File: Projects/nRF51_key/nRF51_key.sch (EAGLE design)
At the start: 4 parts, among them IC1 FT230XQ, X1 USBPCB

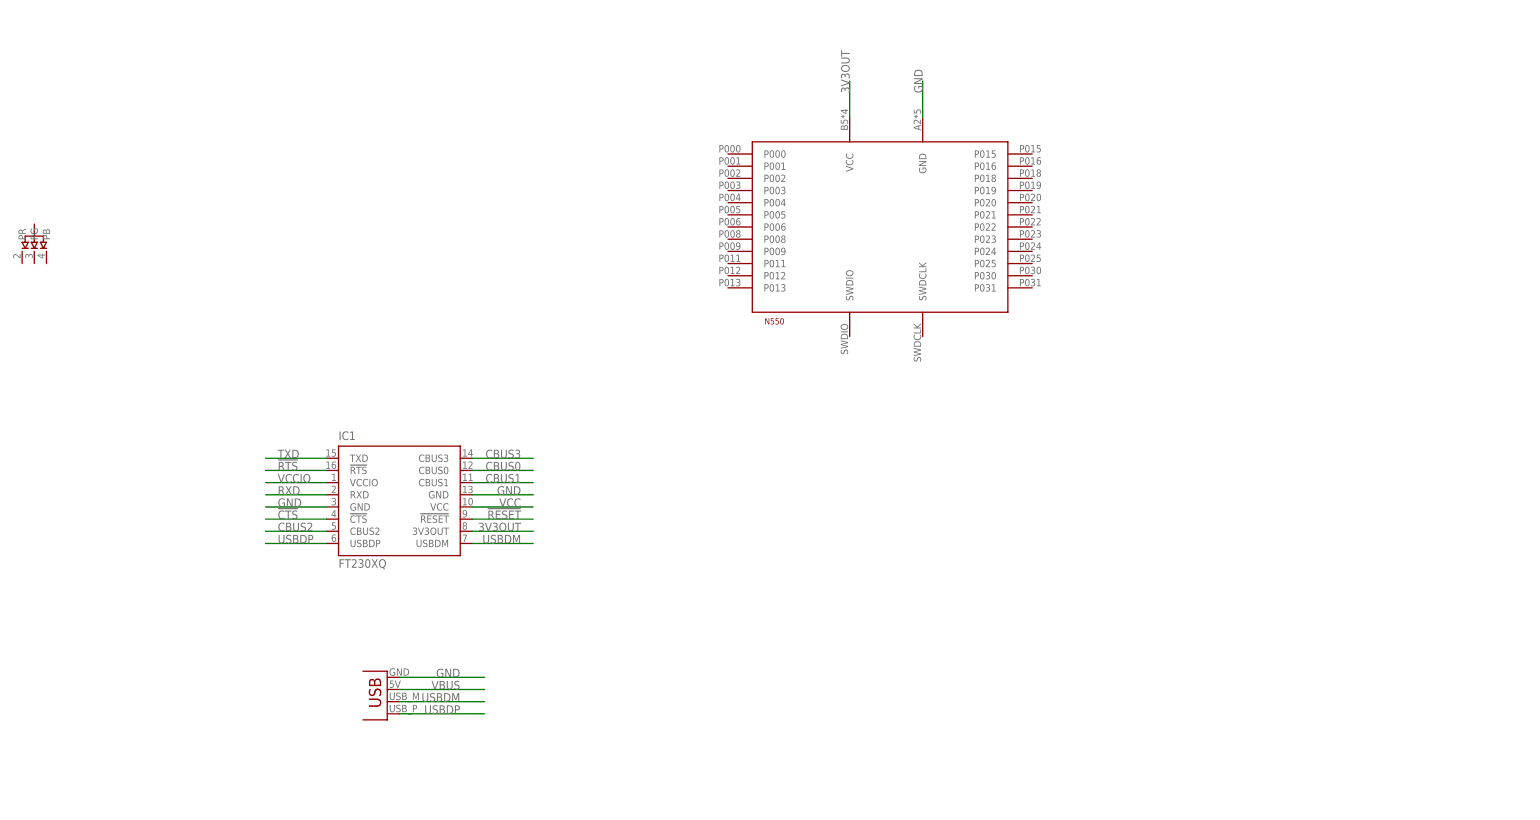
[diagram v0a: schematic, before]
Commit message: More on the nRF51 USB key
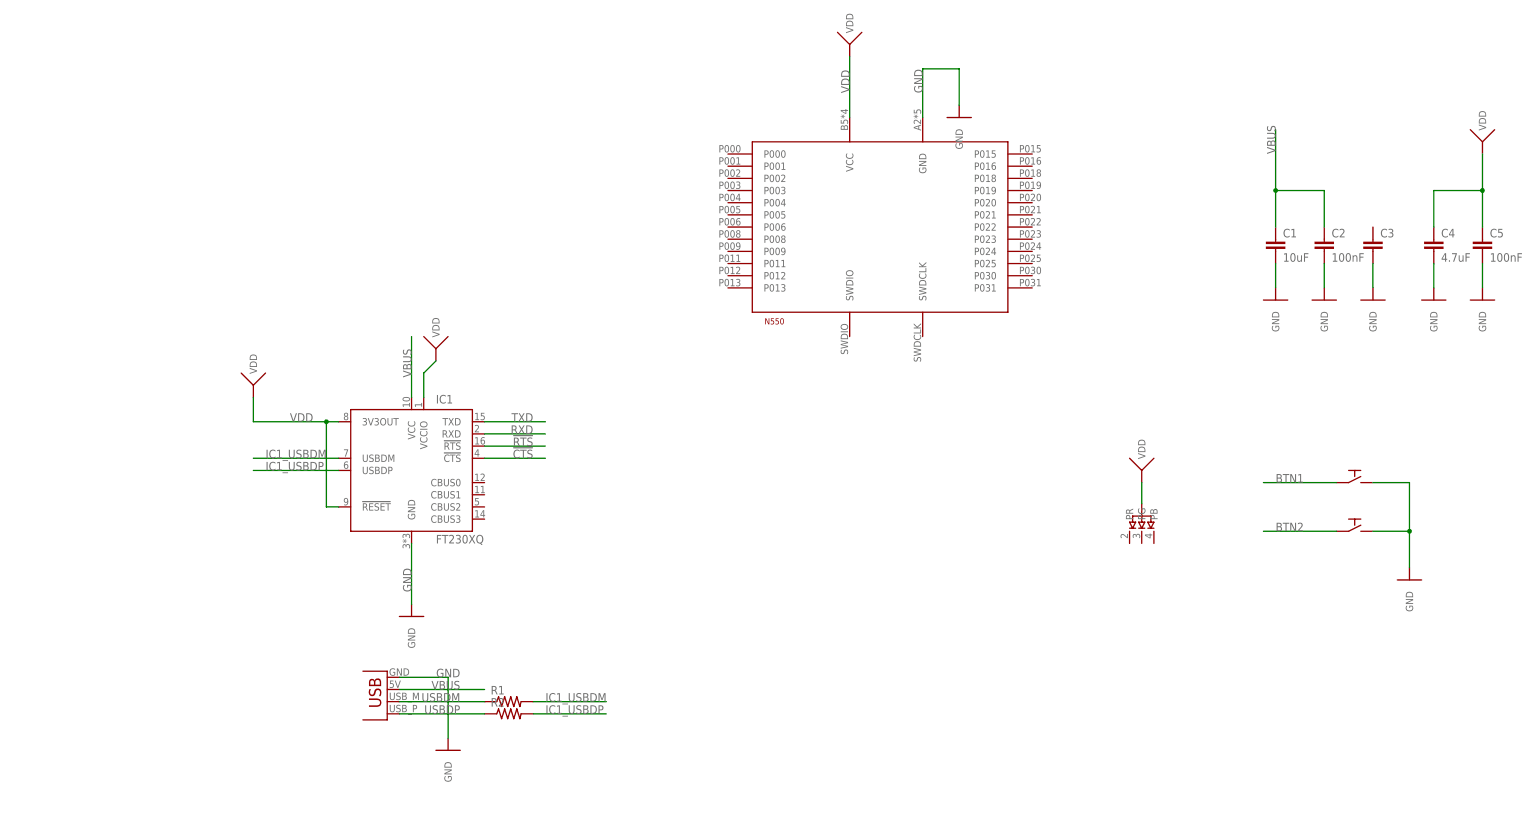
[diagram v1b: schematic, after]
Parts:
- added C1: 10uF, Passives:CAPACITOR0603
- added C2, C5: 100nF, Passives:CAPACITOR0603
- added C3: (no value), Passives:CAPACITOR0603
- added C4: 4.7uF, Passives:CAPACITOR0603
- added R1, R2: (no value), Passives:RESISTOR0603
- added SPST1, SPST2: PTS526SK08, SPST:PTS526SK08
- IC1: device ftdichip:FT230XQ -> FTDI:FT230XQ
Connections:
- removed net !RESET: IC1.!RESET
- removed net 3V3OUT: IC1.3V3OUT, U$1.VCC
- removed net CBUS0: IC1.CBUS0
- removed net CBUS1: IC1.CBUS1
- removed net CBUS2: IC1.CBUS2
- removed net CBUS3: IC1.CBUS3
- removed net VCC: IC1.VCC
- removed net VCCIO: IC1.VCCIO
- new net BTN1: SPST1.P$1
- new net BTN2: SPST2.P$1
- new net IC1_USBDM: IC1.USBDM, R1.2
- new net IC1_USBDP: IC1.USBDP, R2.2
- new net VDD: C4.1, C5.1, D1.P$1, IC1.!RESET, IC1.3V3OUT, IC1.VCCIO, U$1.VCC
- net GND: now also C1.2, C2.2, C3.2, C4.2, C5.2, SPST1.P$2, SPST2.P$2; no longer IC1.GND@1
- net USBDM: now also R1.1; no longer IC1.USBDM
- net USBDP: now also R2.1; no longer IC1.USBDP
- net VBUS: now also C1.1, C2.1, IC1.VCC

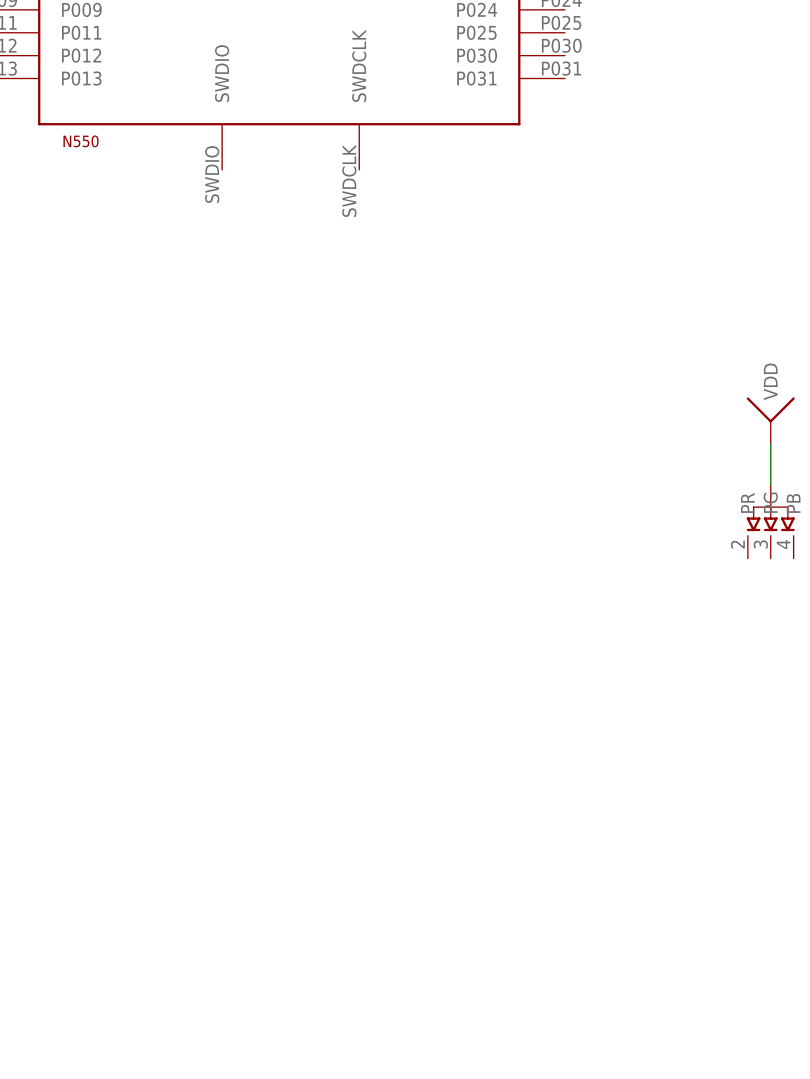
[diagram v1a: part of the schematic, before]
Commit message: Added PCB SD card symbol
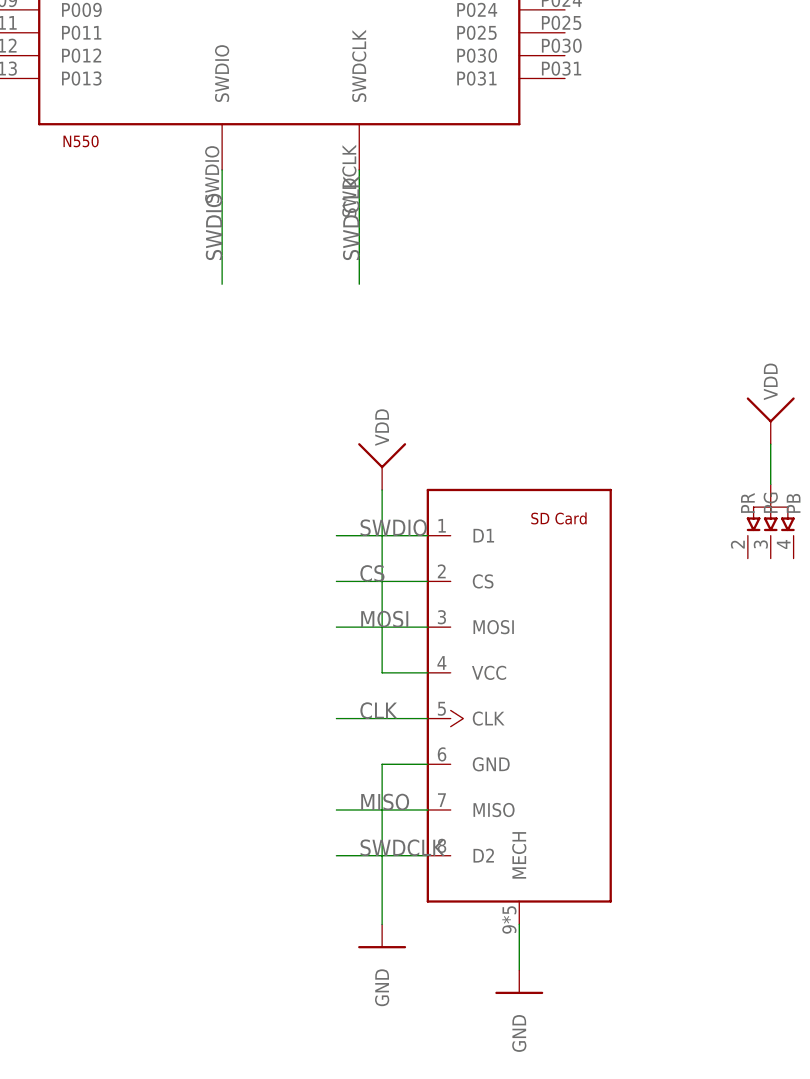
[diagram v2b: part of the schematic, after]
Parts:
- added J1: 47571-0001, SD_Card:47571-0001
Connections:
- new net CLK: J1.CLK
- new net CS: J1.CS
- new net MISO: J1.MISO
- new net MOSI: J1.MOSI
- new net SWDCLK: J1.D2, U$1.SWDCLK
- new net SWDIO: J1.D1, U$1.SWDIO
- net GND: now also J1.GND, J1.MECH
- net VDD: now also J1.VCC
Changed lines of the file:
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@@
 <layer number="54" name="bGND_GNDA" color="1" fill="9" visible="no" active="no"/>
 <layer number="56" name="wert" color="7" fill="1" visible="no" active="no"/>
+<layer number="57" name="tCAD" color="7" fill="1" visible="no" active="no"/>
+<layer number="59" name="tCarbon" color="7" fill="1" visible="no" active="no"/>
+<layer number="60" name="bCarbon" color="7" fill="1" visible="no" active="no"/>
 <layer number="88" name="SimResults" color="9" fill="1" visible="yes" active="yes"/>
 <layer number="89" name="SimProbes" color="9" fill="1" visible="yes" active="yes"/>
@@
 <layer number="125" name="_tNames" color="7" fill="1" visible="no" active="yes"/>
 <layer number="126" name="BIFRNTMAT" color="7" fill="1" visible="yes" active="yes"/>
+<layer number="127" name="_tValues" color="7" fill="1" visible="no" active="no"/>
+<layer number="128" name="_bValues" color="7" fill="1" visible="no" active="no"/>
+<layer number="129" name="Mask" color="7" fill="1" visible="no" active="no"/>
 <layer number="130" name="SMDSTROOK" color="7" fill="1" visible="yes" active="yes"/>
 <layer number="131" name="tAdjust" color="7" fill="1" visible="yes" active="yes"/>
 <layer number="132" name="bAdjust" color="7" fill="1" visible="yes" active="yes"/>
 <layer number="144" name="Drill_legend" color="7" fill="1" visible="no" active="yes"/>
+<layer number="150" name="Notes" color="7" fill="1" visible="no" active="no"/>
 <layer number="151" name="HeatSink" color="7" fill="1" visible="no" active="yes"/>
+<layer number="152" name="_bDocu" color="7" fill="1" visible="no" active="no"/>
+<layer number="153" name="FabDoc1" color="7" fill="1" visible="no" active="no"/>
+<layer number="154" name="FabDoc2" color="7" fill="1" visible="no" active="no"/>
+<layer number="155" name="FabDoc3" color="7" fill="1" visible="no" active="no"/>
 <layer number="199" name="Contour" color="7" fill="1" visible="yes" active="yes"/>
 <layer number="200" name="200bmp" color="1" fill="10" visible="no" active="yes"/>
@@
 <layer number="223" name="223bmp" color="24" fill="1" visible="no" active="no"/>
 <layer number="224" name="224bmp" color="25" fill="1" visible="no" active="no"/>
+<layer number="225" name="225bmp" color="7" fill="1" visible="no" active="no"/>
+<layer number="226" name="226bmp" color="7" fill="1" visible="no" active="no"/>
+<layer number="227" name="227bmp" color="7" fill="1" visible="no" active="no"/>
+<layer number="228" name="228bmp" color="7" fill="1" visible="no" active="no"/>
+<layer number="229" name="229bmp" color="7" fill="1" visible="no" active="no"/>
+<layer number="230" name="230bmp" color="7" fill="1" visible="no" active="no"/>
+<layer number="231" name="231bmp" color="7" fill="1" visible="no" active="no"/>
+<layer number="232" name="Eagle3D_PG2" color="7" fill="1" visible="no" active="no"/>
+<layer number="233" name="Eagle3D_PG3" color="7" fill="1" visible="no" active="no"/>
+<layer number="248" name="Housing" color="7" fill="1" visible="no" active="no"/>
+<layer number="249" name="Edge" color="7" fill="1" visible="no" active="no"/>
 <layer number="250" name="Descript" color="3" fill="1" visible="no" active="no"/>
 <layer number="251" name="SMDround" color="12" fill="11" visible="no" active="no"/>
@@
 <part name="R2" library="Passives" deviceset="RESISTOR" device="0603"/>
 <part name="U$15" library="PowerSupplies" deviceset="VDD" device=""/>
+<part name="J1" library="SD_Card" deviceset="47571-0001" device=""/>
+<part name="U$16" library="PowerSupplies" deviceset="GND" device=""/>
+<part name="U$17" library="PowerSupplies" deviceset="GND" device=""/>
+<part name="U$18" library="PowerSupplies" deviceset="VDD" device=""/>
 </parts>
 <sheets>
@@
 </instance>
 <instance part="U$15" gate="G$1" x="-50.8" y="2.54" smashed="yes"/>
+<instance part="J1" gate="G$1" x="68.58" y="-53.34" smashed="yes"/>
+<instance part="U$16" gate="GND" x="68.58" y="-86.36" smashed="yes"/>
+<instance part="U$17" gate="GND" x="53.34" y="-81.28" smashed="yes"/>
+<instance part="U$18" gate="G$1" x="53.34" y="-27.94" smashed="yes"/>
 </instances>
 <busses>
@@
 <pinref part="C1" gate="G$1" pin="2"/>
 <wire x1="124.46" y1="15.24" x2="124.46" y2="20.32" width="0.1524" layer="91" grouprefs="DECAP"/>
+</segment>
+<segment>
+<pinref part="J1" gate="G$1" pin="GND"/>
+<wire x1="58.42" y1="-60.96" x2="53.34" y2="-60.96" width="0.1524" layer="91"/>
+<pinref part="U$17" gate="GND" pin="GND"/>
+<wire x1="53.34" y1="-60.96" x2="53.34" y2="-78.74" width="0.1524" layer="91"/>
+</segment>
+<segment>
+<pinref part="J1" gate="G$1" pin="MECH"/>
+<pinref part="U$16" gate="GND" pin="GND"/>
+<wire x1="68.58" y1="-78.74" x2="68.58" y2="-83.82" width="0.1524" layer="91"/>
 </segment>
 </net>
@@
 <wire x1="-53.34" y1="-2.54" x2="-53.34" y2="-7.62" width="0.1524" layer="91"/>
 </segment>
+<segment>
+<pinref part="U$18" gate="G$1" pin="VDD"/>
+<wire x1="53.34" y1="-30.48" x2="53.34" y2="-50.8" width="0.1524" layer="91"/>
+<pinref part="J1" gate="G$1" pin="VCC"/>
+<wire x1="53.34" y1="-50.8" x2="58.42" y2="-50.8" width="0.1524" layer="91"/>
+</segment>
 </net>
 <net name="BTN1" class="0">
@@
 </segment>
 </net>
+<net name="MISO" class="0">
+<segment>
+<pinref part="J1" gate="G$1" pin="MISO"/>
+<wire x1="58.42" y1="-66.04" x2="48.26" y2="-66.04" width="0.1524" layer="91"/>
+<label x="50.8" y="-66.04" size="1.778" layer="95"/>
+</segment>
+</net>
+<net name="CLK" class="0">
+<segment>
+<pinref part="J1" gate="G$1" pin="CLK"/>
+<wire x1="58.42" y1="-55.88" x2="48.26" y2="-55.88" width="0.1524" layer="91"/>
+<label x="50.8" y="-55.88" size="1.778" layer="95"/>
+</segment>
+</net>
+<net name="MOSI" class="0">
+<segment>
+<pinref part="J1" gate="G$1" pin="MOSI"/>
+<wire x1="58.42" y1="-45.72" x2="48.26" y2="-45.72" width="0.1524" layer="91"/>
+<label x="50.8" y="-45.72" size="1.778" layer="95"/>
+</segment>
+</net>
+<net name="CS" class="0">
+<segment>
+<pinref part="J1" gate="G$1" pin="CS"/>
+<wire x1="58.42" y1="-40.64" x2="48.26" y2="-40.64" width="0.1524" layer="91"/>
+<label x="50.8" y="-40.64" size="1.778" layer="95"/>
+</segment>
+</net>
+<net name="SWDIO" class="0">
+<segment>
+<pinref part="U$1" gate="G$1" pin="SWDIO"/>
+<wire x1="35.56" y1="5.08" x2="35.56" y2="-7.62" width="0.1524" layer="91"/>
+<label x="35.56" y="-5.08" size="1.778" layer="95" rot="R90"/>
+</segment>
+<segment>
+<pinref part="J1" gate="G$1" pin="D1"/>
+<wire x1="58.42" y1="-35.56" x2="48.26" y2="-35.56" width="0.1524" layer="91"/>
+<label x="50.8" y="-35.56" size="1.778" layer="95"/>
+</segment>
+</net>
+<net name="SWDCLK" class="0">
+<segment>
+<pinref part="U$1" gate="G$1" pin="SWDCLK"/>
+<wire x1="50.8" y1="5.08" x2="50.8" y2="-7.62" width="0.1524" layer="91"/>
+<label x="50.8" y="-5.08" size="1.778" layer="95" rot="R90"/>
+</segment>
+<segment>
+<pinref part="J1" gate="G$1" pin="D2"/>
+<wire x1="58.42" y1="-71.12" x2="48.26" y2="-71.12" width="0.1524" layer="91"/>
+<label x="50.8" y="-71.12" size="1.778" layer="95"/>
+</segment>
+</net>

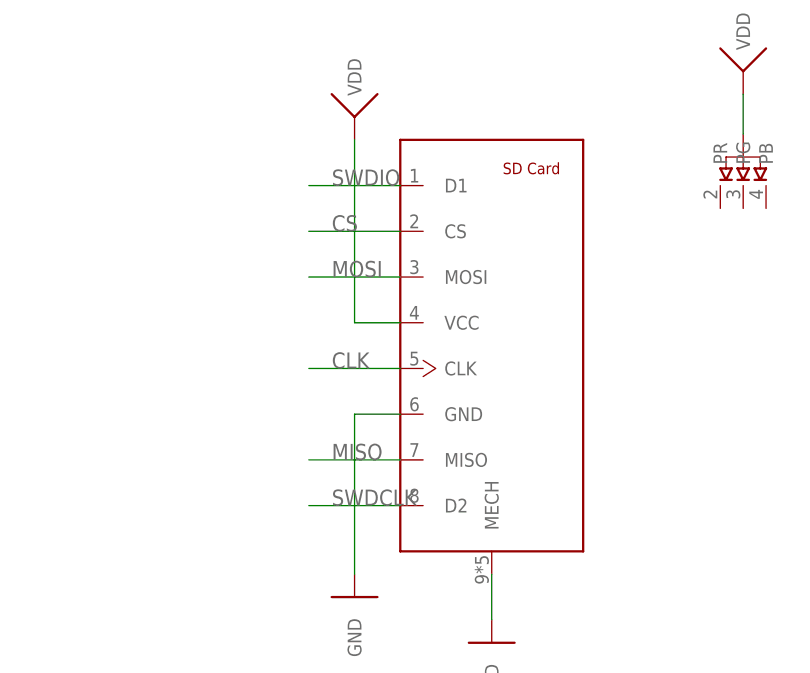
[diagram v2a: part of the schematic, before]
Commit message: Corrected SD card library
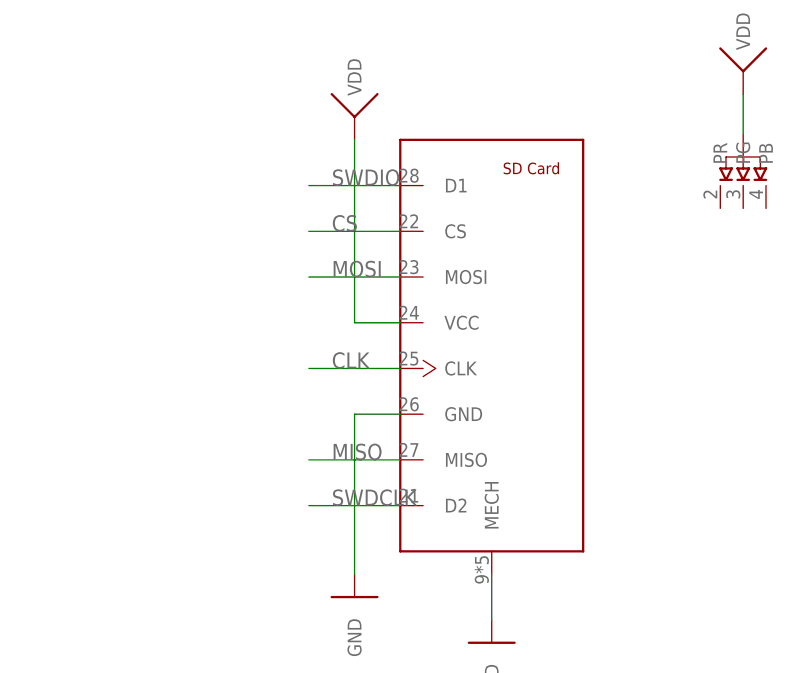
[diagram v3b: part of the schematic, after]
